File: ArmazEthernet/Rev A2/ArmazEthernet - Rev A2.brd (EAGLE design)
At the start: 72 x 80 mm, 138 parts, among them J1 22-05-7028-02, P1 RB1-125BAG1A, U1 LM317MDCY, U2 LM317MDCY, U3 KSZ8995MA, U4 AT24C02C-SSHM-B, X1 NE8FAV, X2 NE8FAV, Y1 8Z-25.000MHZMAAJ-T

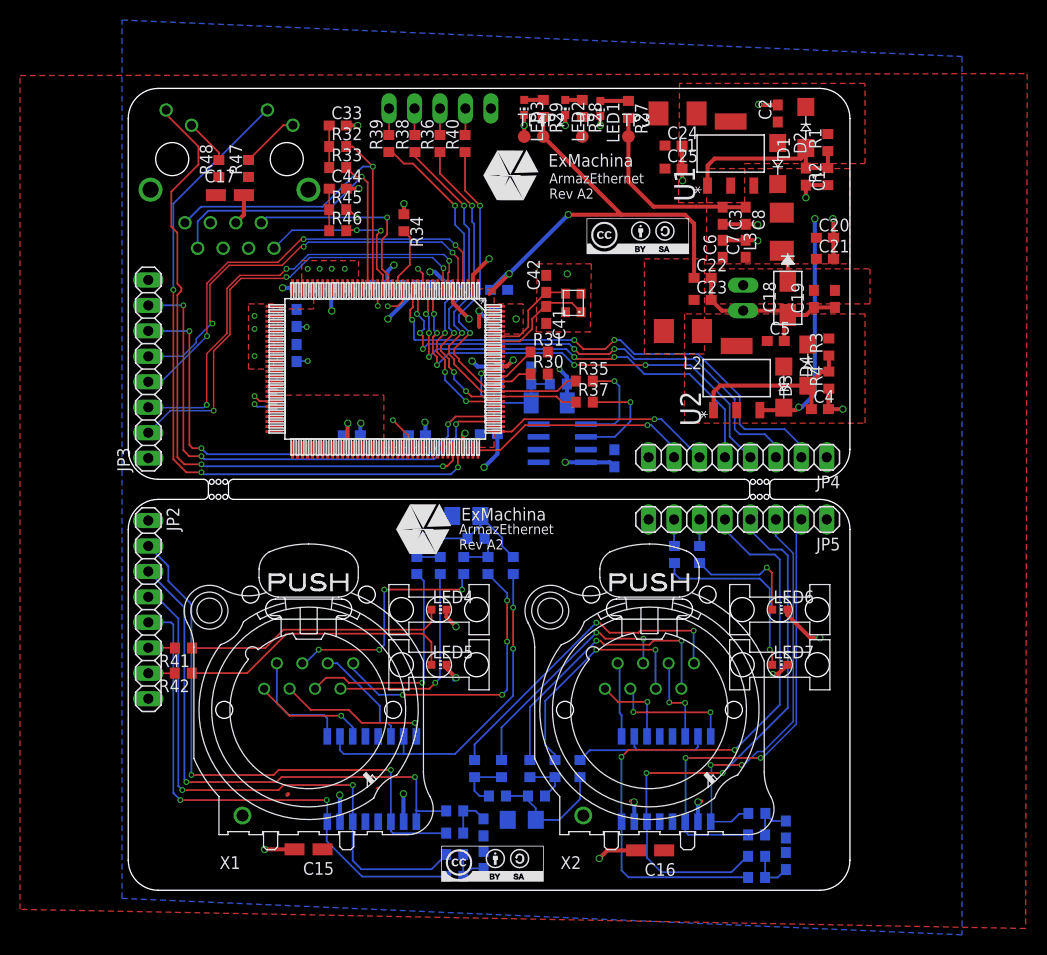
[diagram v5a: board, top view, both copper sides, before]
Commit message: Add condos between the ground of NE8FAV and the gnd
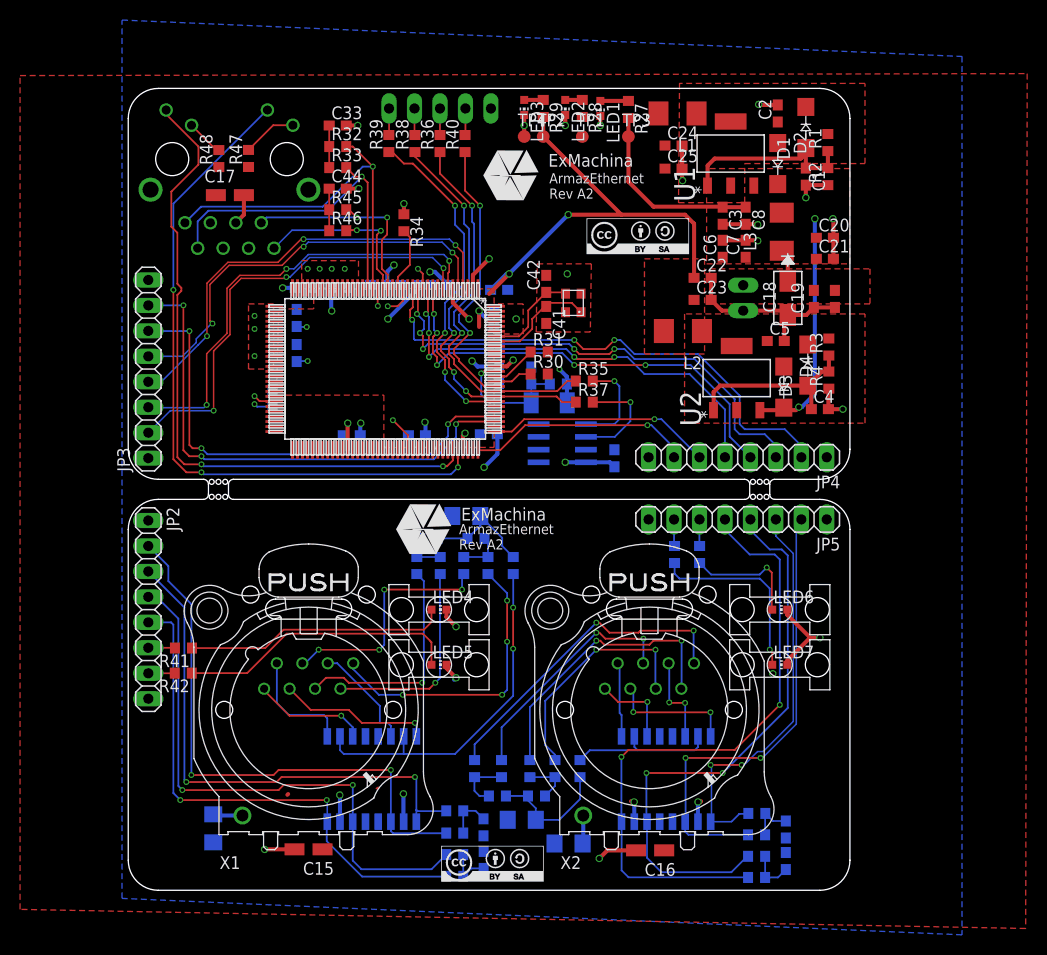
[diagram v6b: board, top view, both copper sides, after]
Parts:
- added C46, C47: 1000pF, 2kV, rcl:C1206
- moved R47 1.00 mm to (12.0, 73.0)
- moved R48 1.00 mm to (9.04, 73.0)
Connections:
- new net N$36: C47.1, X2.G
- new net N$37: C46.1, X1.G
- net GND: now also C46.2, C47.2
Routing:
- net N$37: track 0.00 -> 2.97 mm
- net N$36: track 0.00 -> 2.82 mm
- net GND: track 98.2 -> 100.0 mm
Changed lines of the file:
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@@
 <grid distance="1" unitdist="mm" unit="mm" style="dots" multiple="1" display="yes" altdistance="0.01" altunitdist="mm" altunit="mm"/>
 <layers>
-<layer number="1" name="Top" color="4" fill="1" visible="no" active="yes"/>
+<layer number="1" name="Top" color="4" fill="1" visible="yes" active="yes"/>
 <layer number="2" name="Route2" color="1" fill="3" visible="no" active="no"/>
 <layer number="3" name="Route3" color="4" fill="3" visible="no" active="no"/>
@@
 <layer number="18" name="Vias" color="2" fill="1" visible="yes" active="yes"/>
 <layer number="19" name="Unrouted" color="6" fill="1" visible="yes" active="yes"/>
-<layer number="20" name="Dimension" color="15" fill="1" visible="yes" active="yes"/>
+<layer number="20" name="Dimension" color="15" fill="1" visible="no" active="yes"/>
 <layer number="21" name="tPlace" color="7" fill="1" visible="no" active="yes"/>
 <layer number="22" name="bPlace" color="7" fill="1" visible="yes" active="yes"/>
@@
 <layer number="40" name="bKeepout" color="1" fill="11" visible="no" active="yes"/>
 <layer number="41" name="tRestrict" color="4" fill="10" visible="no" active="yes"/>
-<layer number="42" name="bRestrict" color="1" fill="10" visible="no" active="yes"/>
+<layer number="42" name="bRestrict" color="1" fill="10" visible="yes" active="yes"/>
 <layer number="43" name="vRestrict" color="2" fill="10" visible="no" active="yes"/>
 <layer number="44" name="Drills" color="7" fill="1" visible="no" active="yes"/>
@@
 <text x="33" y="34" size="1.016" layer="21">ArmazEthernet
 Rev A2</text>
+<polygon width="0.4064" layer="41">
+<vertex x="25" y="27"/>
+<vertex x="25" y="21"/>
+<vertex x="28" y="18"/>
+<vertex x="30" y="18"/>
+<vertex x="31" y="17"/>
+<vertex x="31" y="11"/>
+<vertex x="13" y="11"/>
+<vertex x="13" y="27"/>
+</polygon>
+<polygon width="0.4064" layer="42">
+<vertex x="13" y="27"/>
+<vertex x="25" y="27"/>
+<vertex x="25" y="21"/>
+<vertex x="28" y="18"/>
+<vertex x="30" y="18"/>
+<vertex x="31" y="17"/>
+<vertex x="30.98" y="13.54"/>
+<vertex x="12.98" y="13.54"/>
+</polygon>
+<polygon width="0.4064" layer="42" pour="hatch">
+<vertex x="45" y="27"/>
+<vertex x="45" y="14"/>
+<vertex x="59" y="14"/>
+<vertex x="59" y="27"/>
+</polygon>
+<polygon width="0.4064" layer="41" pour="hatch">
+<vertex x="45" y="27"/>
+<vertex x="45" y="10"/>
+<vertex x="59" y="10"/>
+<vertex x="59" y="27"/>
+</polygon>
 </plain>
 <attributes>
@@
 <element name="R46" library="rcl" package="R0603" value="49.9" x="20.9" y="65.8"/>
 <element name="C44" library="rcl" package="C0603" value="0.1uF" x="20.9" y="70"/>
-<element name="R47" library="rcl" package="R0603" value="220" x="12" y="72.01" rot="R90"/>
-<element name="R48" library="rcl" package="R0603" value="220" x="9.04" y="72" rot="R90"/>
+<element name="R47" library="rcl" package="R0603" value="220" x="12" y="73.01" rot="R90"/>
+<element name="R48" library="rcl" package="R0603" value="220" x="9.04" y="73" rot="R90"/>
 <element name="C45" library="rcl" package="C0603" value="10uF" x="40.21" y="51.36" rot="MR90"/>
 <element name="R49" library="rcl" package="R0603" value="10K" x="42.91" y="50.51" rot="MR180"/>
 <element name="U$9" library="diode" package="SOD-123_MINI-SMA" value="1N4148W" x="42" y="48.63" rot="MR0"/>
 <element name="U$10" library="cc-by-sa" package="CC-BY-SA" value="CC-BY-SA" x="36.5" y="3.1"/>
+<element name="C46" library="rcl" package="C1206" value="1000pF, 2kV" x="8.48" y="6.18" rot="MR270"/>
+<element name="C47" library="rcl" package="C1206" value="1000pF, 2kV" x="43.93" y="4.67" rot="MR0"/>
 </elements>
 <signals>
@@
 <contactref element="JP4" pad="8"/>
 <contactref element="JP2" pad="8"/>
-<via x="64.3" y="21.6" extent="1-16" drill="0.35" diameter="0.4064"/>
+<via x="64.3" y="21.6" extent="1-16" drill="0.5" diameter="0.4064"/>
 <wire x1="64.3" y1="21.6" x2="64.4" y2="21.5" width="0.1778" layer="16"/>
 <wire x1="64.4" y1="21.5" x2="64.5" y2="21.5" width="0.1778" layer="16"/>
@@
 <wire x1="31.75" y1="22.5" x2="31.75" y2="22.15" width="0.4064" layer="1"/>
 <wire x1="31.75" y1="22.15" x2="32.7" y2="21.2" width="0.4064" layer="1"/>
-<wire x1="64.3" y1="21.6" x2="64.85" y2="21.6" width="0.4064" layer="1"/>
-<wire x1="64.85" y1="21.6" x2="65.75" y2="22.5" width="0.4064" layer="1"/>
 <wire x1="68.03" y1="25.2" x2="65.75" y2="27.48" width="0.4064" layer="1"/>
 <wire x1="65.75" y1="27.48" x2="65.75" y2="28" width="0.4064" layer="1"/>
@@
 <wire x1="13.6126" y1="4.0876" x2="13.6" y2="4.075" width="0.4064" layer="1"/>
 <contactref element="C45" pad="2"/>
+<wire x1="65.75" y1="22.5" x2="65.75" y2="22.92" width="0.4064" layer="1"/>
+<wire x1="65.75" y1="22.92" x2="68.03" y2="25.2" width="0.4064" layer="1"/>
+<contactref element="C46" pad="2"/>
+<contactref element="C47" pad="2"/>
 <wire x1="51.91" y1="37" x2="51.91" y2="43.2" width="0" layer="19" extent="1-1"/>
 </signal>
@@
 <wire x1="64.5" y1="33.5" x2="65" y2="33" width="0.1778" layer="16"/>
 <wire x1="65" y1="33" x2="65" y2="18.5" width="0.1778" layer="16"/>
-<wire x1="65" y1="18.5" x2="60.5" y2="14" width="0.1778" layer="16"/>
-<via x="60.5" y="14" extent="1-16" drill="0.35" diameter="0.4064"/>
 <wire x1="60.5" y1="14" x2="49.9" y2="14" width="0.1778" layer="1"/>
 <wire x1="49.9" y1="14" x2="49.2" y2="13.3" width="0.1778" layer="1"/>
@@
 <wire x1="59.53" y1="43.2" x2="59.53" y2="47.97" width="0.1778" layer="16"/>
 <wire x1="49.215" y1="6.8455" x2="49.215" y2="7.2455" width="0.15" layer="16"/>
+<via x="65" y="18.5" extent="1-16" drill="0.35"/>
+<wire x1="60.5" y1="14" x2="65" y2="18.5" width="0.1778" layer="1"/>
 <wire x1="59.53" y1="37" x2="59.53" y2="43.2" width="0" layer="19" extent="1-1"/>
 </signal>
@@
 <contactref element="R48" pad="2"/>
 <contactref element="P1" pad="L3"/>
-<wire x1="9.04" y1="72.85" x2="9.04" y2="73.59835" width="0.1778" layer="1"/>
+<wire x1="9.04" y1="73.85" x2="9.04" y2="73.59835" width="0.1778" layer="1"/>
 <wire x1="9.04" y1="73.59835" x2="6.31441875" y2="76.32393125" width="0.1778" layer="1"/>
 </signal>
@@
 <contactref element="R47" pad="2"/>
 <contactref element="P1" pad="L1"/>
-<wire x1="12" y1="72.86" x2="15.46443125" y2="76.32443125" width="0.1778" layer="1"/>
-<wire x1="15.46443125" y1="76.32443125" x2="16.42626875" y2="76.32443125" width="0.1778" layer="1"/>
+<wire x1="12" y1="73.86" x2="14.46443125" y2="76.32443125" width="0.1778" layer="1"/>
+<wire x1="14.46443125" y1="76.32443125" x2="16.42626875" y2="76.32443125" width="0.1778" layer="1"/>
+</signal>
+<signal name="N$36">
+<contactref element="C47" pad="1"/>
+<contactref element="X2" pad="G"/>
+<wire x1="45.396" y1="7.459" x2="45.396" y2="4.736" width="0.4064" layer="16"/>
+<wire x1="45.396" y1="4.736" x2="45.33" y2="4.67" width="0.4064" layer="16"/>
+</signal>
+<signal name="N$37">
+<contactref element="X1" pad="G"/>
+<contactref element="C46" pad="1"/>
+<wire x1="11.396" y1="7.459" x2="8.601" y2="7.459" width="0.4064" layer="16"/>
+<wire x1="8.601" y1="7.459" x2="8.48" y2="7.58" width="0.4064" layer="16"/>
 </signal>
 </signals>

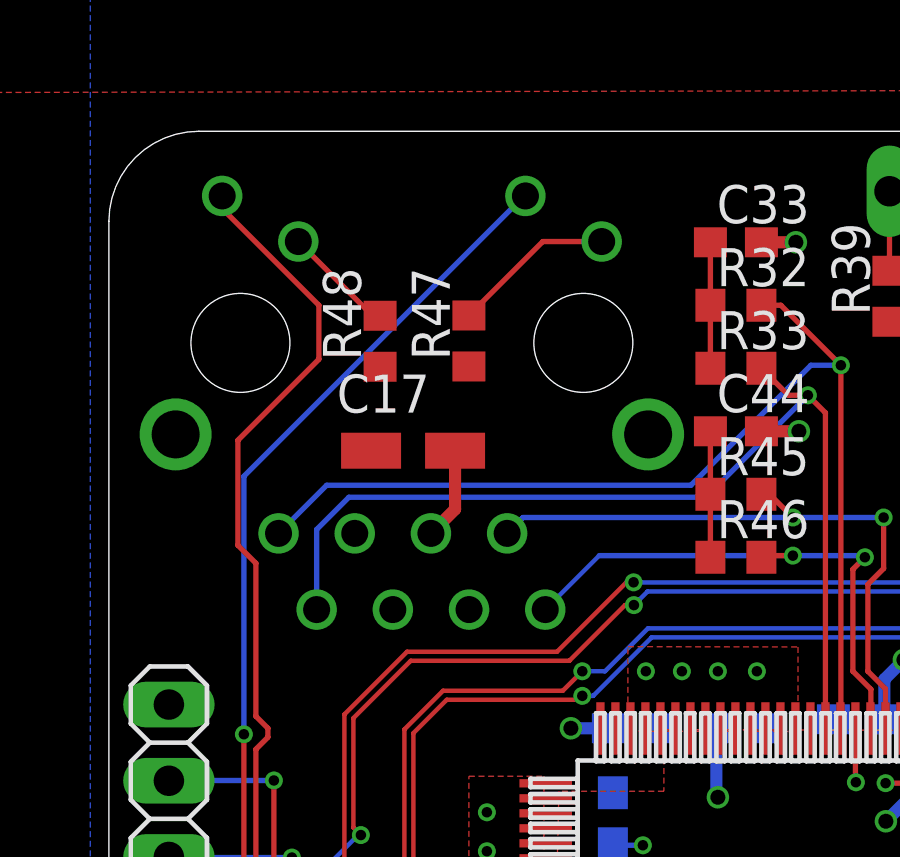
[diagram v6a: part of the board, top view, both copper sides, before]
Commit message: Add restric near Magjack
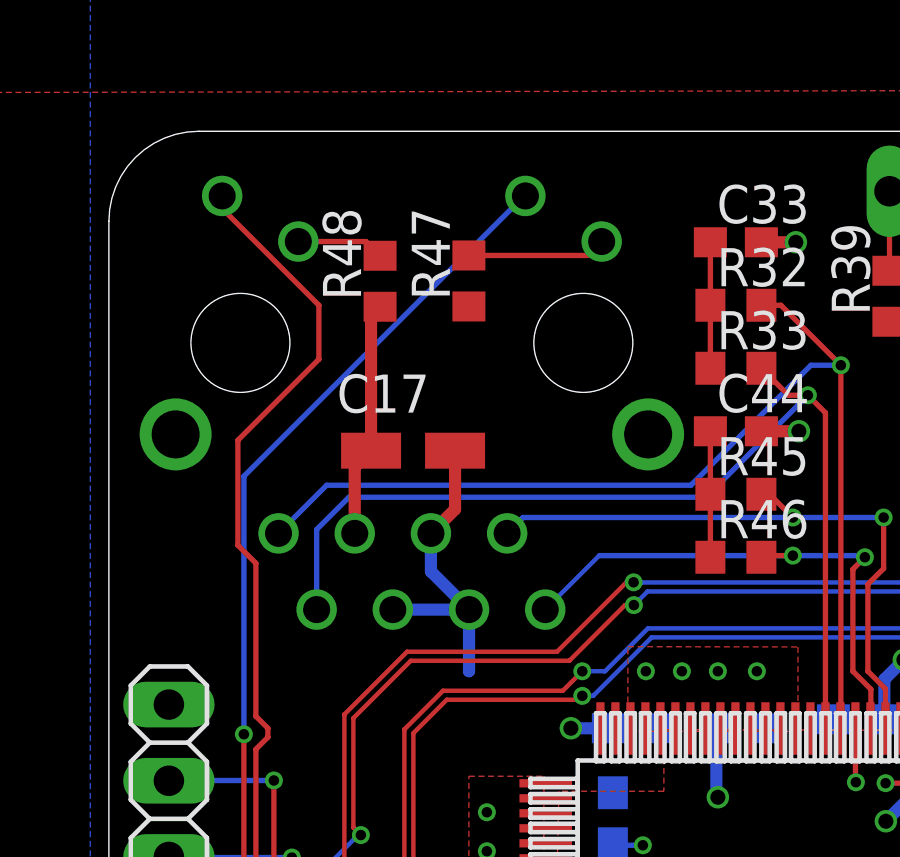
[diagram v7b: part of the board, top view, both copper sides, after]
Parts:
- moved R47 2.00 mm to (12.0, 75.0)
- moved R48 2.00 mm to (9.04, 75.0)
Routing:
- net +3V3: track 32.1 -> 40.0 mm
- net GND: track 100.0 -> 107.7 mm
- net N$34: track 4.11 -> 3.17 mm
- net N$35: track 5.45 -> 4.62 mm
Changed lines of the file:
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@@
 <layer number="19" name="Unrouted" color="6" fill="1" visible="yes" active="yes"/>
 <layer number="20" name="Dimension" color="15" fill="1" visible="no" active="yes"/>
-<layer number="21" name="tPlace" color="7" fill="1" visible="no" active="yes"/>
+<layer number="21" name="tPlace" color="7" fill="1" visible="yes" active="yes"/>
 <layer number="22" name="bPlace" color="7" fill="1" visible="yes" active="yes"/>
-<layer number="23" name="tOrigins" color="15" fill="1" visible="no" active="yes"/>
+<layer number="23" name="tOrigins" color="15" fill="1" visible="yes" active="yes"/>
 <layer number="24" name="bOrigins" color="15" fill="1" visible="yes" active="yes"/>
-<layer number="25" name="tNames" color="7" fill="1" visible="no" active="yes"/>
+<layer number="25" name="tNames" color="7" fill="1" visible="yes" active="yes"/>
 <layer number="26" name="bNames" color="7" fill="1" visible="yes" active="yes"/>
-<layer number="27" name="tValues" color="7" fill="1" visible="no" active="yes"/>
+<layer number="27" name="tValues" color="7" fill="1" visible="yes" active="yes"/>
 <layer number="28" name="bValues" color="7" fill="1" visible="yes" active="yes"/>
 <layer number="29" name="tStop" color="7" fill="3" visible="no" active="yes"/>
@@
 <layer number="39" name="tKeepout" color="4" fill="11" visible="no" active="yes"/>
 <layer number="40" name="bKeepout" color="1" fill="11" visible="no" active="yes"/>
-<layer number="41" name="tRestrict" color="4" fill="10" visible="no" active="yes"/>
+<layer number="41" name="tRestrict" color="4" fill="10" visible="yes" active="yes"/>
 <layer number="42" name="bRestrict" color="1" fill="10" visible="yes" active="yes"/>
 <layer number="43" name="vRestrict" color="2" fill="10" visible="no" active="yes"/>
@@
 <layer number="49" name="Reference" color="7" fill="1" visible="no" active="yes"/>
 <layer number="50" name="dxf" color="7" fill="1" visible="no" active="yes"/>
-<layer number="51" name="tDocu" color="7" fill="1" visible="no" active="yes"/>
+<layer number="51" name="tDocu" color="7" fill="1" visible="yes" active="yes"/>
 <layer number="52" name="bDocu" color="7" fill="1" visible="yes" active="yes"/>
 <layer number="53" name="tGND_GNDA" color="7" fill="1" visible="no" active="yes"/>
@@
 <vertex x="59" y="10"/>
 <vertex x="59" y="27"/>
+</polygon>
+<polygon width="0.4064" layer="41" pour="hatch">
+<vertex x="2" y="73"/>
+<vertex x="2" y="63"/>
+<vertex x="19" y="63"/>
+<vertex x="19" y="73"/>
+</polygon>
+<polygon width="0.4064" layer="42" pour="hatch">
+<vertex x="2" y="73"/>
+<vertex x="19" y="73"/>
+<vertex x="19" y="63"/>
+<vertex x="2" y="63"/>
 </polygon>
 </plain>
@@
 <element name="R46" library="rcl" package="R0603" value="49.9" x="20.9" y="65.8"/>
 <element name="C44" library="rcl" package="C0603" value="0.1uF" x="20.9" y="70"/>
-<element name="R47" library="rcl" package="R0603" value="220" x="12" y="73.01" rot="R90"/>
-<element name="R48" library="rcl" package="R0603" value="220" x="9.04" y="73" rot="R90"/>
+<element name="R47" library="rcl" package="R0603" value="220" x="12" y="75.01" rot="R90"/>
+<element name="R48" library="rcl" package="R0603" value="220" x="9.04" y="75" rot="R90"/>
 <element name="C45" library="rcl" package="C0603" value="10uF" x="40.21" y="51.36" rot="MR90"/>
 <element name="R49" library="rcl" package="R0603" value="10K" x="42.91" y="50.51" rot="MR180"/>
@@
 <via x="43.02" y="51.98" extent="1-16" drill="0.35"/>
 <wire x1="43.02" y1="51.98" x2="43" y2="52" width="0.4064" layer="1"/>
+<wire x1="8.195009375" y1="66.595840625" x2="8.195009375" y2="68.806409375" width="0.4064" layer="1"/>
+<wire x1="8.195009375" y1="68.806409375" x2="8.74" y2="69.3514" width="0.4064" layer="1"/>
+<wire x1="8.74" y1="69.3514" x2="8.74" y2="73.85" width="0.4064" layer="1"/>
+<wire x1="8.74" y1="73.85" x2="9.04" y2="74.15" width="0.4064" layer="1"/>
 <wire x1="2" y1="36.89" x2="2" y2="43.11" width="0" layer="19" extent="1-1"/>
 </signal>
@@
 <contactref element="C46" pad="2"/>
 <contactref element="C47" pad="2"/>
+<wire x1="10.735009375" y1="66.595840625" x2="10.735009375" y2="65.325840625" width="0.4064" layer="16"/>
+<wire x1="10.735009375" y1="65.325840625" x2="12.005009375" y2="64.055840625" width="0.4064" layer="16"/>
+<wire x1="9.465009375" y1="64.055840625" x2="12.005009375" y2="64.055840625" width="0.4064" layer="16"/>
+<wire x1="12.005009375" y1="64.055840625" x2="12.005009375" y2="62.005009375" width="0.4064" layer="16"/>
+<wire x1="12.005009375" y1="62.005009375" x2="12" y2="62" width="0.4064" layer="16"/>
 <wire x1="51.91" y1="37" x2="51.91" y2="43.2" width="0" layer="19" extent="1-1"/>
 </signal>
@@
 <contactref element="R48" pad="2"/>
 <contactref element="P1" pad="L3"/>
-<wire x1="9.04" y1="73.85" x2="9.04" y2="73.59835" width="0.1778" layer="1"/>
-<wire x1="9.04" y1="73.59835" x2="6.31441875" y2="76.32393125" width="0.1778" layer="1"/>
+<wire x1="9.04" y1="75.85" x2="9.04" y2="75.59835" width="0.1778" layer="1"/>
+<wire x1="6.31441875" y1="76.32393125" x2="8.56606875" y2="76.32393125" width="0.1778" layer="1"/>
+<wire x1="8.56606875" y1="76.32393125" x2="9.04" y2="75.85" width="0.1778" layer="1"/>
 </signal>
 <signal name="N$35">
 <contactref element="R47" pad="2"/>
 <contactref element="P1" pad="L1"/>
-<wire x1="12" y1="73.86" x2="14.46443125" y2="76.32443125" width="0.1778" layer="1"/>
-<wire x1="14.46443125" y1="76.32443125" x2="16.42626875" y2="76.32443125" width="0.1778" layer="1"/>
+<wire x1="12" y1="75.86" x2="15.9618375" y2="75.86" width="0.1778" layer="1"/>
+<wire x1="15.9618375" y1="75.86" x2="16.42626875" y2="76.32443125" width="0.1778" layer="1"/>
 </signal>
 <signal name="N$36">
